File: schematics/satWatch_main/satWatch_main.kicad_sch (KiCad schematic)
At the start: 0 parts

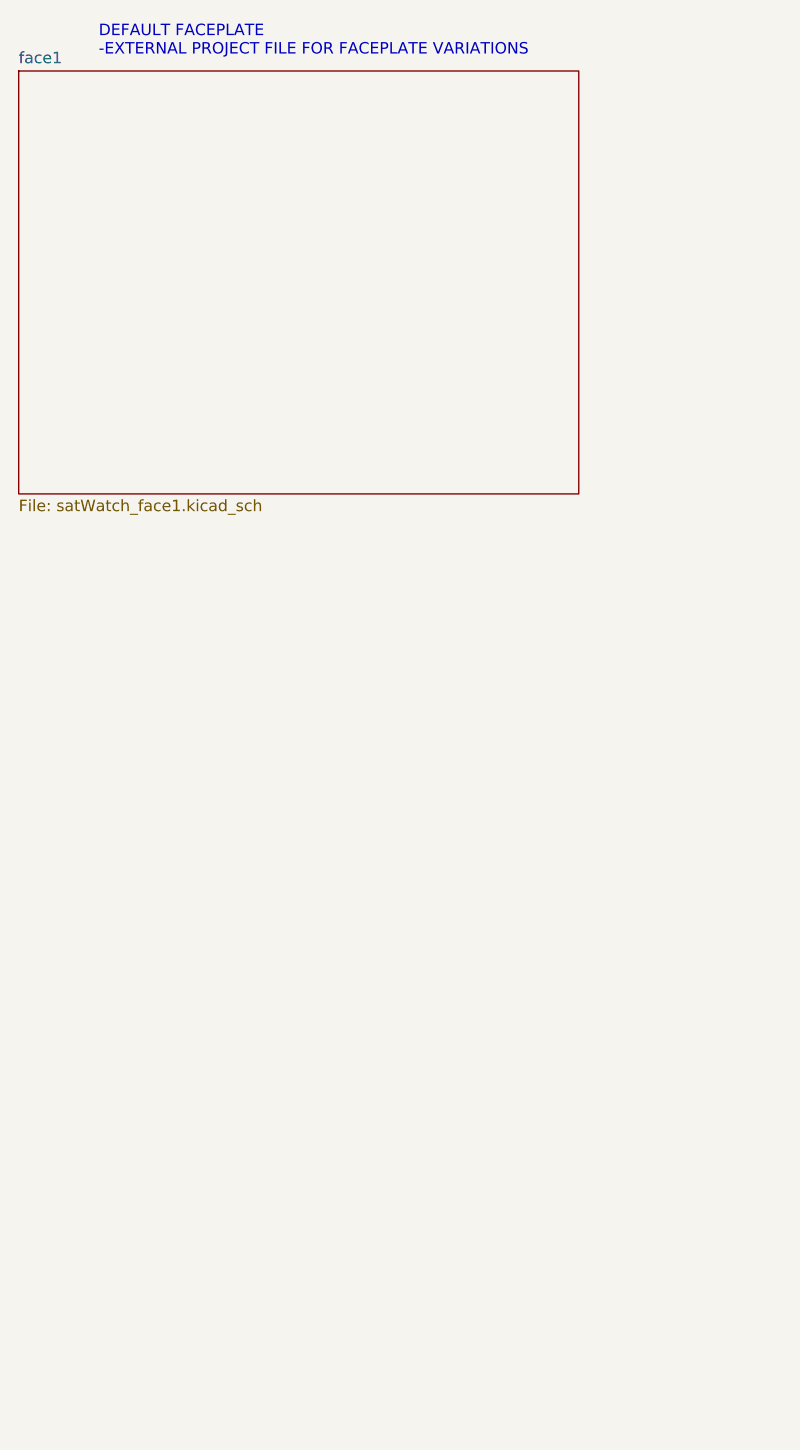
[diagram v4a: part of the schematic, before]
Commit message: v1.2
WIP of major revisions of PCB board. Changed components and layout for better routing
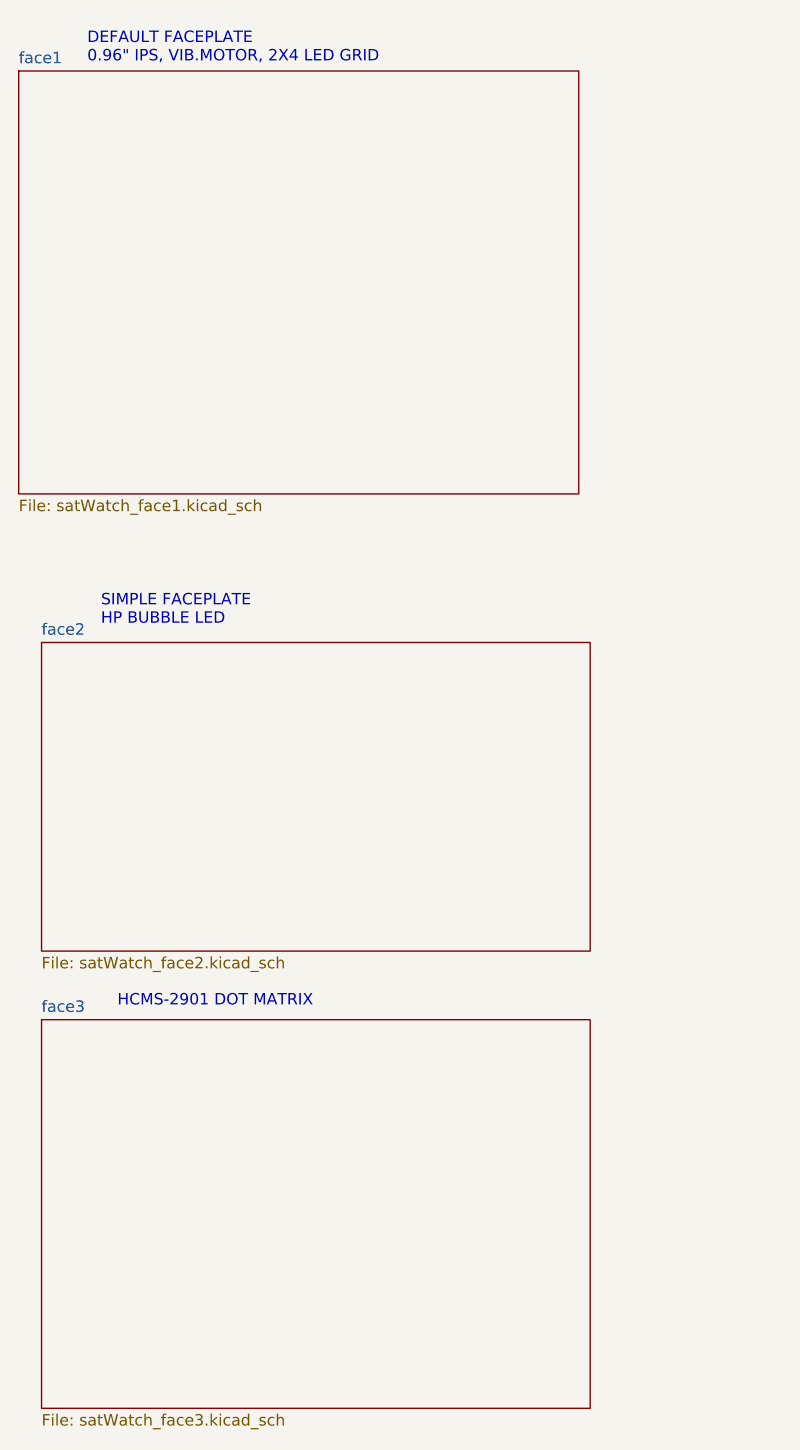
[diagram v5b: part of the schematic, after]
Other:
- added sheet face2 (satWatch_face2.kicad_sch)
- added sheet face3 (satWatch_face3.kicad_sch)
- note added: "DEFAULT FACEPLATE 0.96" IPS, VIB.MOTOR, 2X4 LED GRID"
- note added: "HCMS-2901 DOT MATRIX"
- note added: "SIMPLE FACEPLATE HP BUBBLE LED"
- note removed: "DEFAULT FACEPLATE -EXTERNAL PROJECT FILE FOR FACEPLATE VARIATIONS"
- title: MAINBOARD -> satWatch
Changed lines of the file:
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@@
 	(paper "A3")
 	(title_block
-		(title "MAINBOARD")
-		(rev "0.1")
+		(title "satWatch")
+		(rev "2.0")
 		(company "MECHAMEKA")
-		(comment 1 "MAINBOARD OF WATCHBODY")
-	)
-	(text "DEFAULT FACEPLATE\n-EXTERNAL PROJECT FILE FOR FACEPLATE VARIATIONS\n"
-		(exclude_from_sim no)
-		(at 73.66 90.678 0)
+	)
+	(text "HCMS-2901 DOT MATRIX"
+		(exclude_from_sim no)
+		(at 86.614 197.358 0)
 		(effects
 			(font
 				(size 1.27 1.27)
 			)
+		)
+	)
+	(text "SIMPLE FACEPLATE\nHP BUBBLE LED\n"
+		(exclude_from_sim no)
+		(at 73.914 153.924 0)
+		(effects
+			(font
+				(size 1.27 1.27)
+			)
+			(justify left)
+		)
+	)
+	(text "DEFAULT FACEPLATE\n0.96\" IPS, VIB.MOTOR, 2X4 LED GRID\n"
+		(exclude_from_sim no)
+		(at 72.39 91.44 0)
+		(effects
+			(font
+				(size 1.27 1.27)
+			)
 			(justify left)
 		)
@@
 				)
 			)
+		)
+	)
+	(sheet
+		(at 67.31 199.39)
+		(size 60.96 43.18)
+		(exclude_from_sim no)
+		(in_bom yes)
+		(on_board yes)
+		(dnp no)
+		(fields_autoplaced yes)
+		(stroke
+			(width 0.1524)
+			(type solid)
+		)
+		(fill
+			(color 0 0 0 0)
+		)
+		(property "Sheetname" "face3"
+			(at 67.31 198.6784 0)
+			(show_name no)
+			(do_not_autoplace no)
+			(effects
+				(font
+					(size 1.27 1.27)
+				)
+				(justify left bottom)
+			)
+		)
+		(property "Sheetfile" "satWatch_face3.kicad_sch"
+			(at 67.31 243.1546 0)
+			(show_name no)
+			(do_not_autoplace no)
+			(effects
+				(font
+					(size 1.27 1.27)
+				)
+				(justify left top)
+			)
+		)
+		(instances
+			(project "satWatch_main"
+				(path "/b975a3df-968d-424f-9025-993d668abad1"
+					(page "6")
+				)
+			)
+		)
+	)
+	(sheet
+		(at 67.31 157.48)
+		(size 60.96 34.29)
+		(exclude_from_sim no)
+		(in_bom yes)
+		(on_board yes)
+		(dnp no)
+		(fields_autoplaced yes)
+		(stroke
+			(width 0.1524)
+			(type solid)
+		)
+		(fill
+			(color 0 0 0 0)
+		)
+		(property "Sheetname" "face2"
+			(at 67.31 156.7684 0)
+			(show_name no)
+			(do_not_autoplace no)
+			(effects
+				(font
+					(size 1.27 1.27)
+				)
+				(justify left bottom)
+			)
+		)
+		(property "Sheetfile" "satWatch_face2.kicad_sch"
+			(at 67.31 192.3546 0)
+			(show_name no)
+			(do_not_autoplace no)
+			(effects
+				(font
+					(size 1.27 1.27)
+				)
+				(justify left top)
+			)
+		)
+		(instances
+			(project "satWatch_main"
+				(path "/b975a3df-968d-424f-9025-993d668abad1"
+					(page "4")
+				)
+			)
